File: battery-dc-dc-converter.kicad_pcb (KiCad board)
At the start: 2 copper layers, 42 x 31 mm, 18 parts, among them J1 Conn_01x02, J2 Conn_01x02, U1 LMR16030

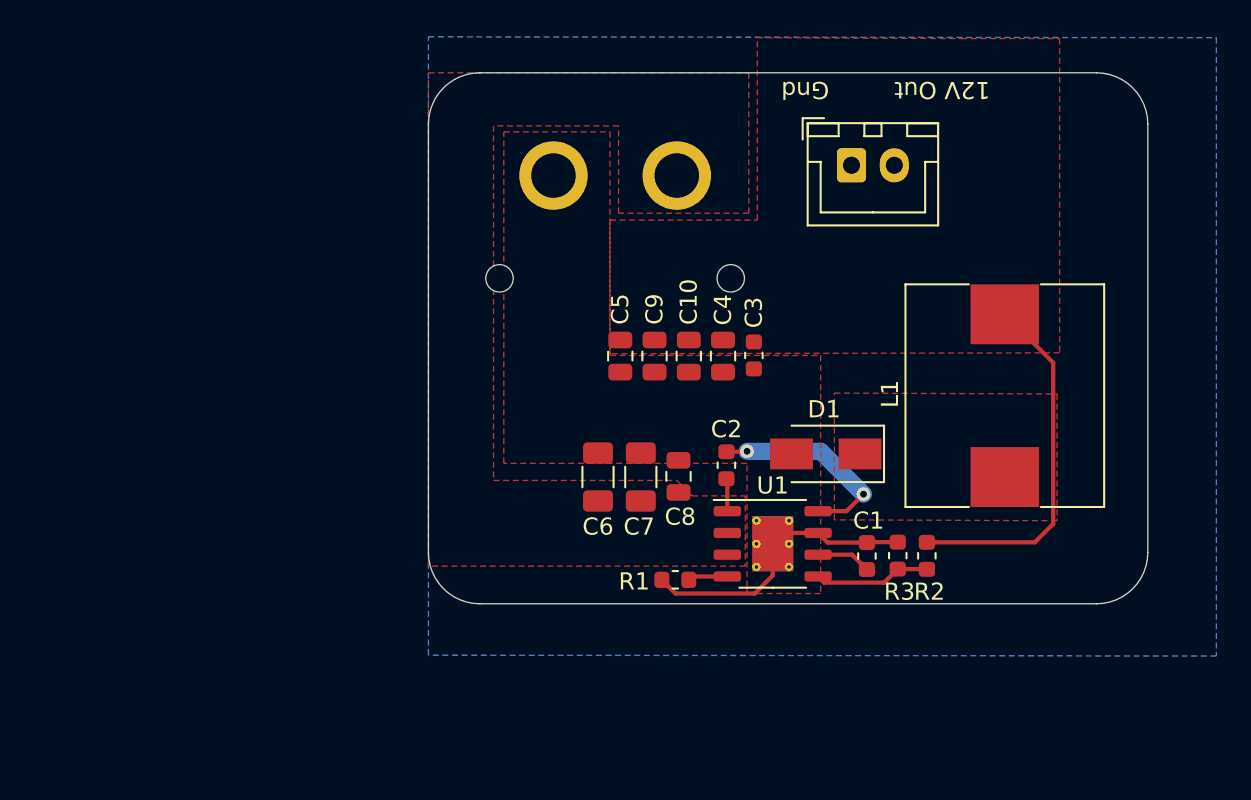
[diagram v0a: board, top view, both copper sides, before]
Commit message: Added fuses
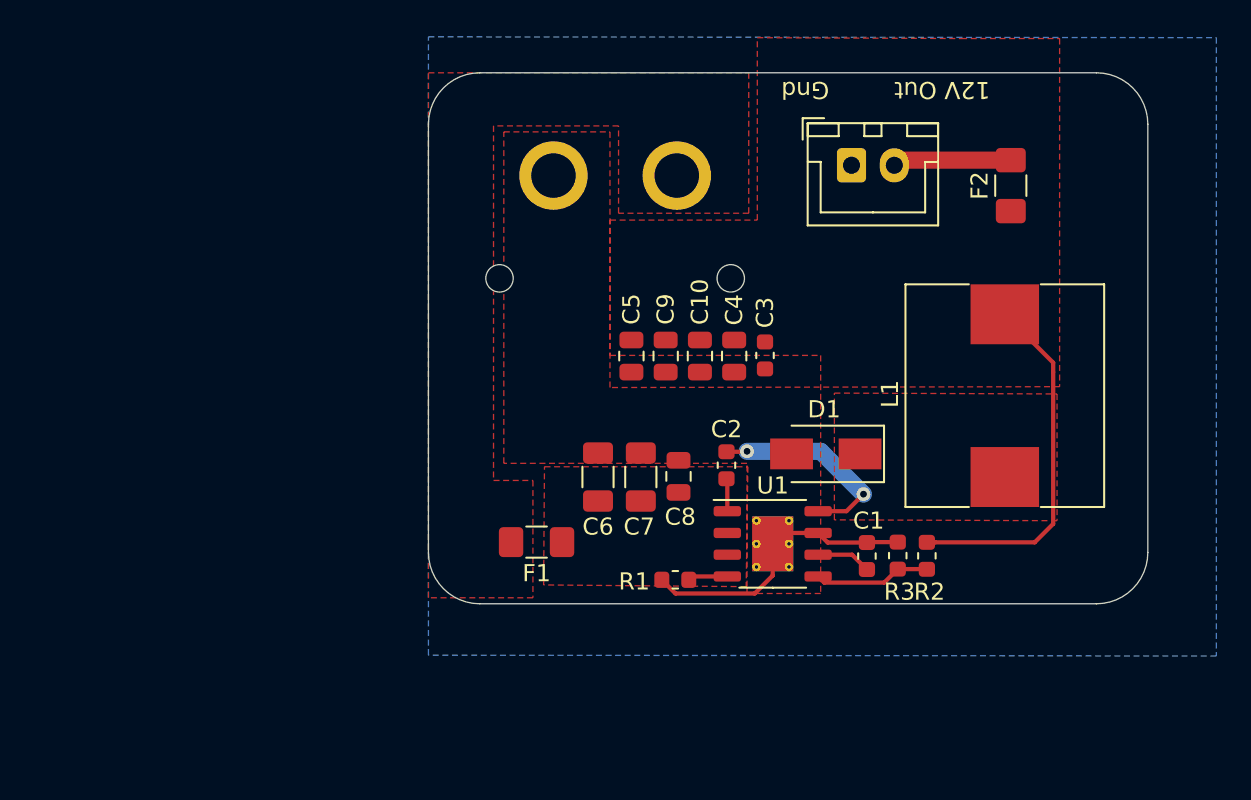
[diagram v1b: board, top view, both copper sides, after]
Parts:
- added F1: 1A, Fuse:Fuse_1206_3216Metric_Pad1.42x1.75mm_HandSolder, F.Cu at (106.3, 63.4)
- added F2: 3A, Fuse:Fuse_1206_3216Metric_Pad1.42x1.75mm_HandSolder, F.Cu at (134.0, 42.6)
- moved C3 0.65 mm to (119.7, 52.5)
- moved C10 0.65 mm to (115.8, 52.5)
- moved C4 0.65 mm to (117.8, 52.5)
- moved C5 0.65 mm to (111.8, 52.5)
- moved C9 0.65 mm to (113.8, 52.5)
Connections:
- J1 pad 2: VCC -> Net-(F1-Pad2)
- J2 pad 2: +12V -> Net-(F2-Pad2)
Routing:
- net Net-(F2-Pad2): track 0.00 -> 6.92 mm
- added copper zone on F.Cu, net Net-(F1-Pad2)

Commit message: Added low voltage protection
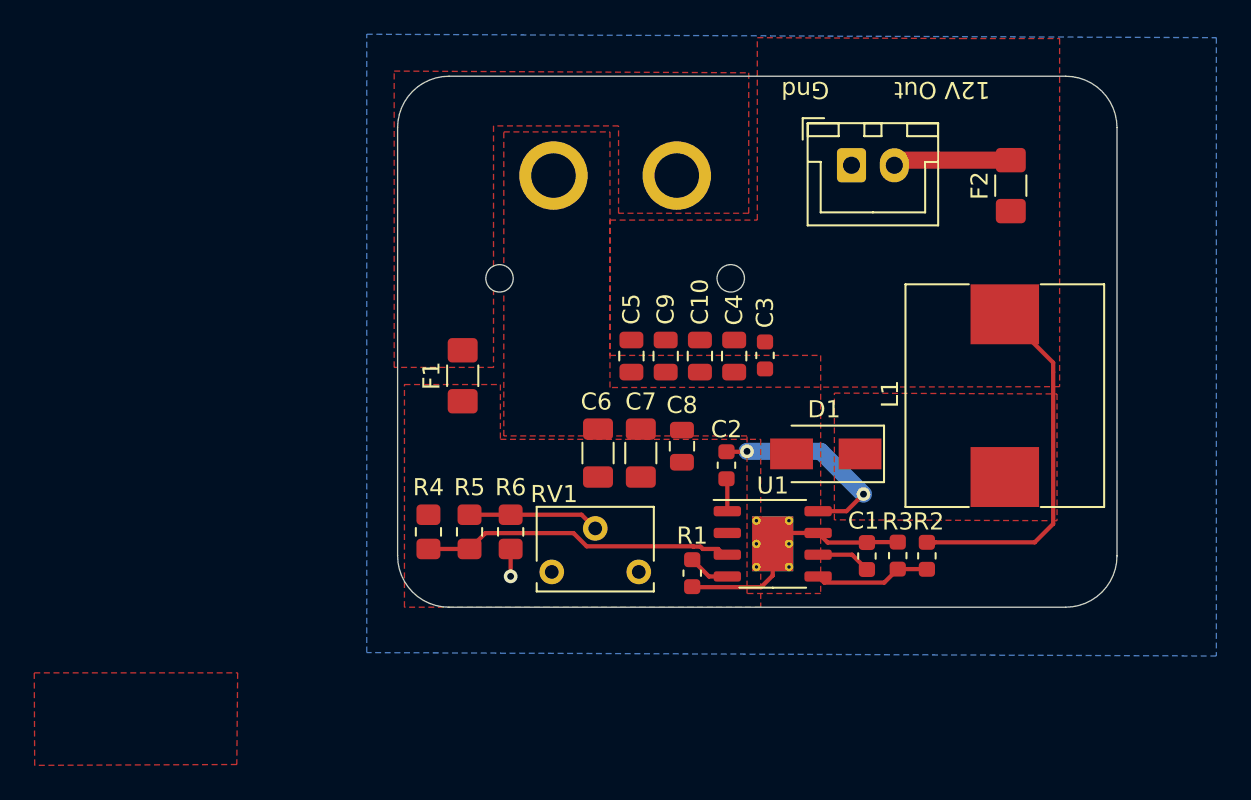
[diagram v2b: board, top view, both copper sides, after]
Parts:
- added R4: 560K, Resistor_SMD:R_0805_2012Metric_Pad1.20x1.40mm_HandSolder, F.Cu at (100.0, 62.8)
- added R5: 18K, Resistor_SMD:R_0805_2012Metric_Pad1.20x1.40mm_HandSolder, F.Cu at (102.4, 62.8)
- added R6: R, Resistor_SMD:R_0805_2012Metric_Pad1.20x1.40mm_HandSolder, F.Cu at (104.8, 62.8)
- added RV1: 10K, Potentiometer_THT:Potentiometer_Vishay_T73XX_Horizontal, F.Cu at (107.2, 65.1)
- moved F1 10.6 mm to (102.0, 53.7), turned to 90 degrees
- moved C8 1.77 mm to (114.8, 57.8)
- moved C6 1.40 mm to (109.9, 58.2)
- moved C7 1.40 mm to (112.4, 58.2)
- moved R1 1.06 mm to (115.4, 65.2), turned to 270 degrees
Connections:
- U1 pad 3: VCC -> Net-(R4-Pad2)
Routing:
- net Net-(R4-Pad2): track 0.00 -> 18.5 mm
- net Net-(R5-Pad2): track 0.00 -> 7.67 mm
- net GND: track 16.9 -> 16.5 mm, vias 0 -> 1

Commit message: Added panelized layout
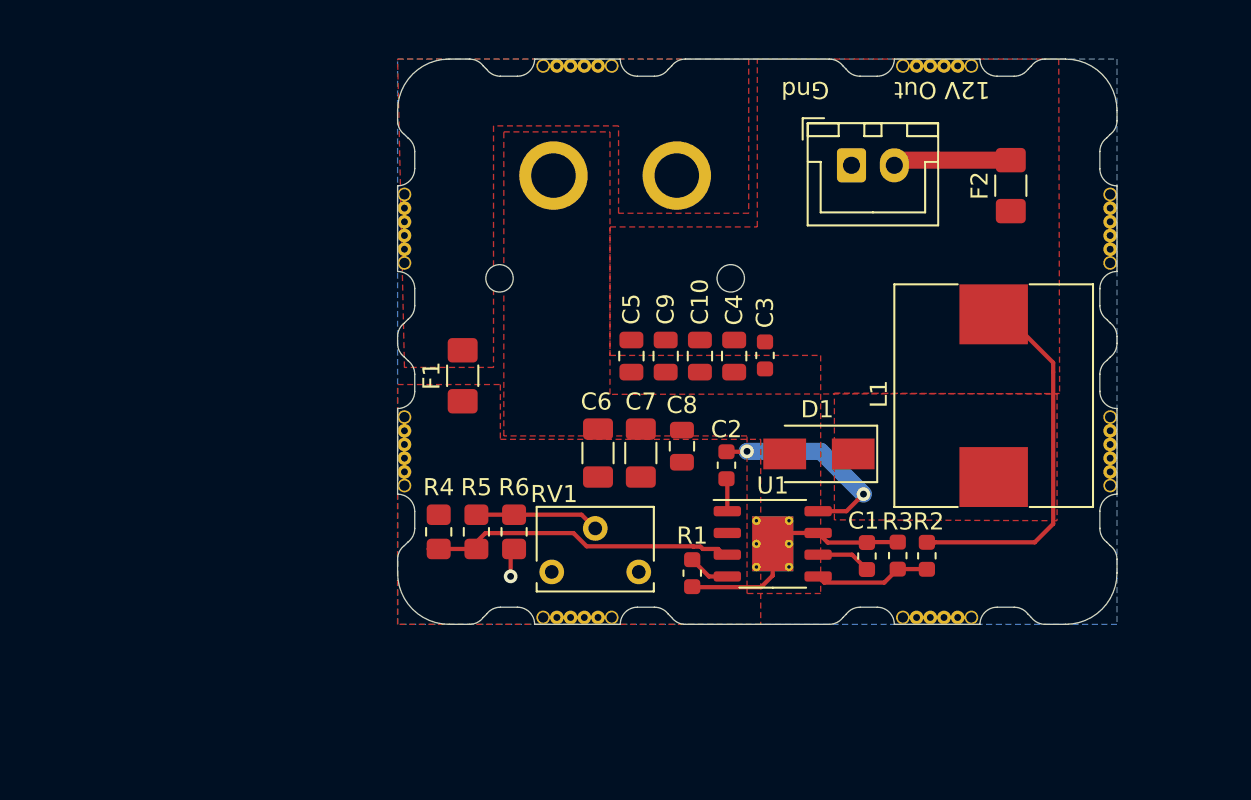
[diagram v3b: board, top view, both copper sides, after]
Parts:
- added REF**: mousebite, scooter-ps:mousebite, F.Cu at (103.2, 35.2)
- added REF**: mousebite, scooter-ps:mousebite, F.Cu at (124.2, 35.2)
- added REF**: mousebite, scooter-ps:mousebite, F.Cu at (140.2, 39.6)
- added REF**: mousebite, scooter-ps:mousebite, F.Cu at (140.2, 52.6)
- added REF**: mousebite, scooter-ps:mousebite, F.Cu at (135.2, 68.2)
- added REF**: mousebite, scooter-ps:mousebite, F.Cu at (114.2, 68.2)
- added REF**: mousebite, scooter-ps:mousebite, F.Cu at (98.2, 63.6)
- added REF**: mousebite, scooter-ps:mousebite, F.Cu at (98.2, 50.6)
- moved L1 0.65 mm to (133.0, 54.9)
- moved R4 0.60 mm to (100.6, 62.8)
- moved D1 0.40 mm to (122.8, 58.2)
- moved R5 0.40 mm to (102.8, 62.8)
- moved R6 0.20 mm to (105.0, 62.8)
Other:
- board size 42 x 31 mm -> 42 x 33 mm

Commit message: Updateed power pads, on/off resistors.
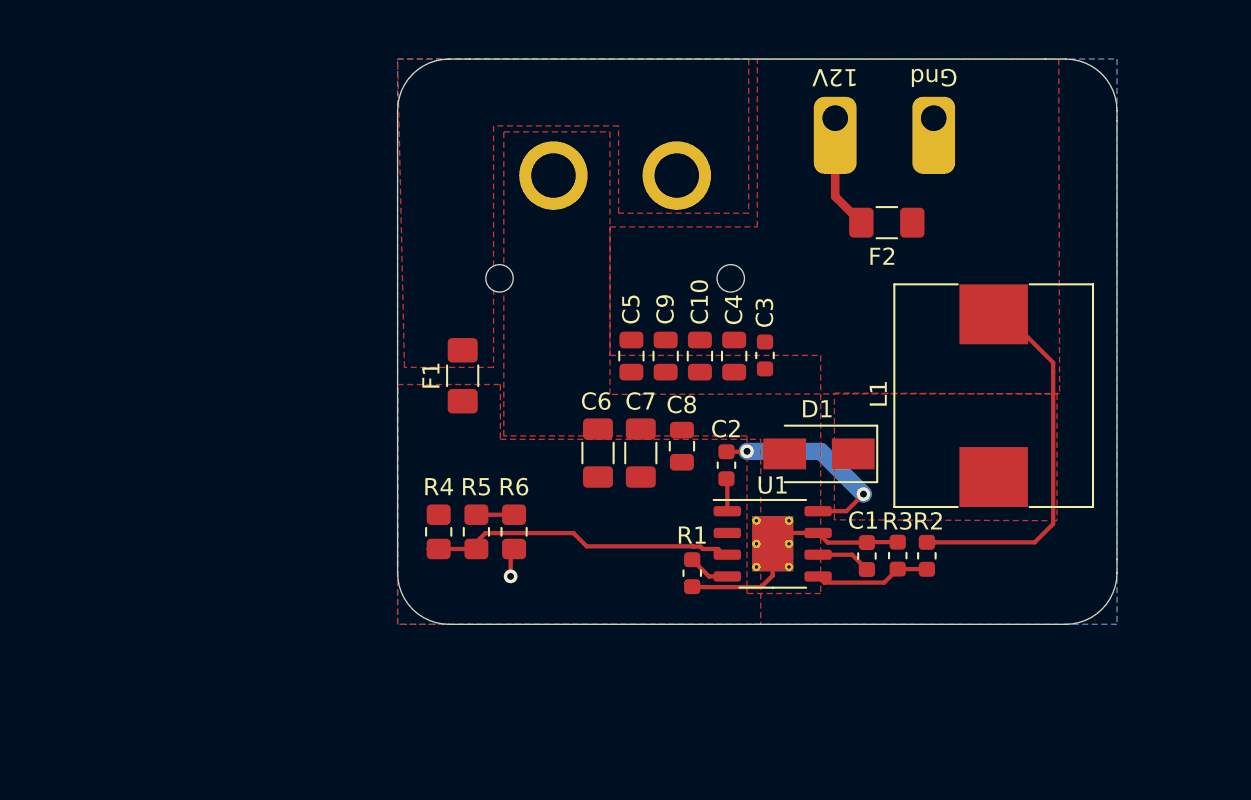
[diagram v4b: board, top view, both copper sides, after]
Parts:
- removed REF** (x8): mousebite, scooter-ps:mousebite
- removed RV1: 10K, Potentiometer_THT:Potentiometer_Vishay_T73XX_Horizontal
- added J3: Conn_01x01, battery-dc-dc-converter:hole-pad, F.Cu at (129.5, 38.8)
- F1: value 1A -> 3A
- J2: value Conn_01x02 -> Conn_01x01; footprint Connector_JST:JST_XH_B2B-XH-A_1x02_P2.50mm_Vertical -> battery-dc-dc-converter:hole-pad
- R4: value 560K -> 1M
- R5: value 18K -> 33K
- R6: value R -> 3k9
- moved F2 7.55 mm to (126.8, 44.8), turned to 0 degrees
- moved J2 2.82 mm to (123.8, 38.8)
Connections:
- F2 pad 1: +12V -> Net-(F2-Pad1)
- F2 pad 2: Net-(F2-Pad2) -> +12V
- J2 pad 1: GND -> Net-(F2-Pad1)
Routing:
- net Net-(F2-Pad1): track 0.00 -> 7.09 mm
- net Net-(F2-Pad2): track 6.92 -> 0.00 mm
- net Net-(R5-Pad2): track 7.67 -> 2.40 mm
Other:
- outline, holes or cut-outs redrawn
- board text added: "12V"
- board text removed: "12V Out"

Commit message: Panalized PCBs
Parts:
- moved J2 0.75 mm to (123.8, 39.5)
- moved J3 0.75 mm to (129.5, 39.5)
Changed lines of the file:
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@@
     (pad_to_mask_clearance 0.05)
     (aux_axis_origin 0 0)
+    (grid_origin 98.25 35.25)
     (visible_elements FFFFFF7F)
     (pcbplotparams
       (layerselection 0x010fc_ffffffff)
-      (usegerberextensions false)
+      (usegerberextensions true)
       (usegerberattributes true)
       (usegerberadvancedattributes true)
@@
       (viasonmask false)
       (mode 1)
-      (useauxorigin false)
+      (useauxorigin true)
       (hpglpennumber 1)
       (hpglpenspeed 20)
@@
       (drillshape 0)
       (scaleselection 1)
-      (outputdirectory "fabrication-output/v2/"))
+      (outputdirectory "fabrication-output/v3/"))
   )
   (net 0 "")
@@
   )
   (module battery-dc-dc-converter:hole-pad (layer F.Cu)
-    (at 129.5 38.75)
+    (at 129.5 39.5)
     (fp_text reference J3 (at 0 0.5) (layer F.SilkS) hide
       (effects (font (size 1 1) (thickness 0.15)))
@@
       (effects (font (size 1 1) (thickness 0.15)))
     )
-    (pad 1 thru_hole roundrect (at 0 -0.1) (size 2.5 4.5) (drill 1.5 (offset 0 1)) (layers *.Cu *.Mask) (roundrect_rratio 0.25)
+    (pad 1 thru_hole roundrect (at 0 -0.1) (size 2.5 4.5) (drill 1.5) (layers *.Cu *.Mask) (roundrect_rratio 0.25)
       (net 2 GND))
   )
   (module battery-dc-dc-converter:hole-pad (layer F.Cu)
-    (at 123.75 38.75)
+    (at 123.75 39.5)
     (fp_text reference J2 (at 0 0.5) (layer F.SilkS) hide
       (effects (font (size 1 1) (thickness 0.15)))
@@
       (effects (font (size 1 1) (thickness 0.15)))
     )
-    (pad 1 thru_hole roundrect (at 0 -0.1) (size 2.5 4.5) (drill 1.5 (offset 0 1)) (layers *.Cu *.Mask) (roundrect_rratio 0.25)
+    (pad 1 thru_hole roundrect (at 0 -0.1) (size 2.5 4.5) (drill 1.5) (layers *.Cu *.Mask) (roundrect_rratio 0.25)
       (net 12 "Net-(F2-Pad1)"))
   )

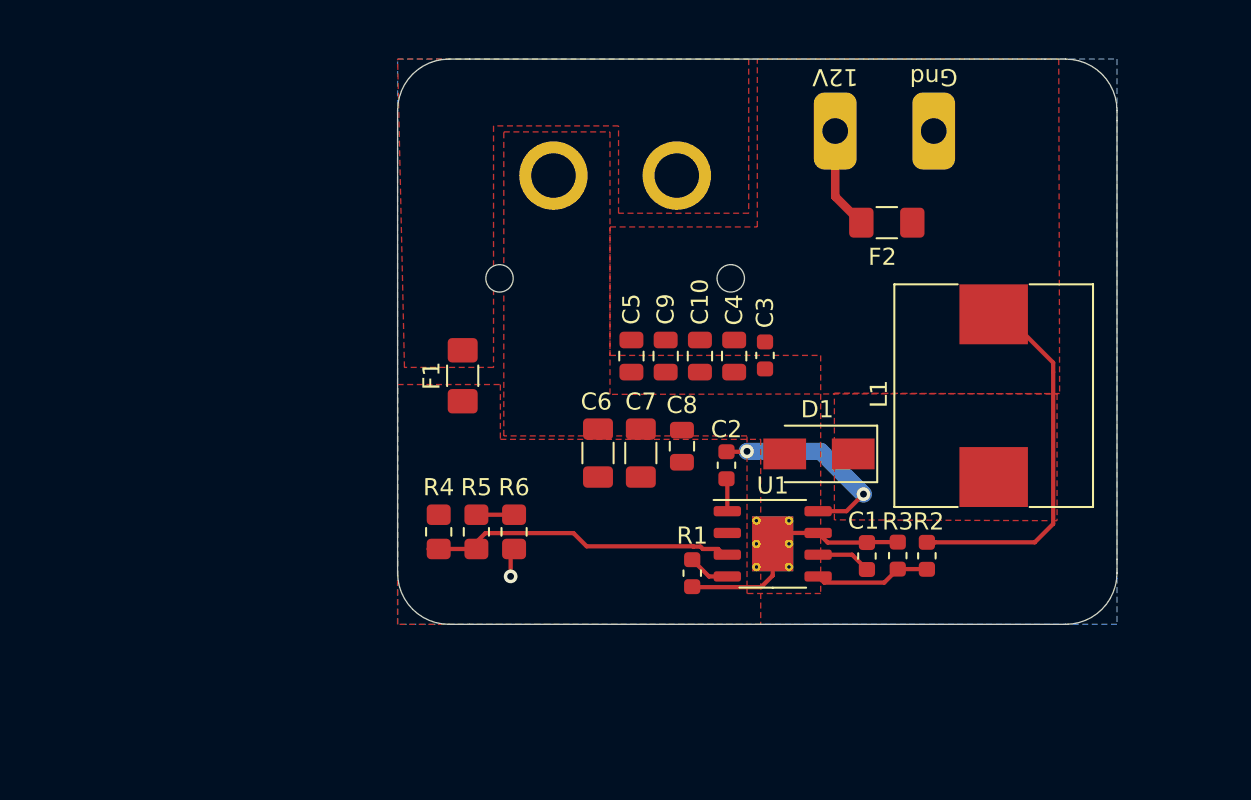
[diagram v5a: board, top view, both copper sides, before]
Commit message: Added recessed nibbles
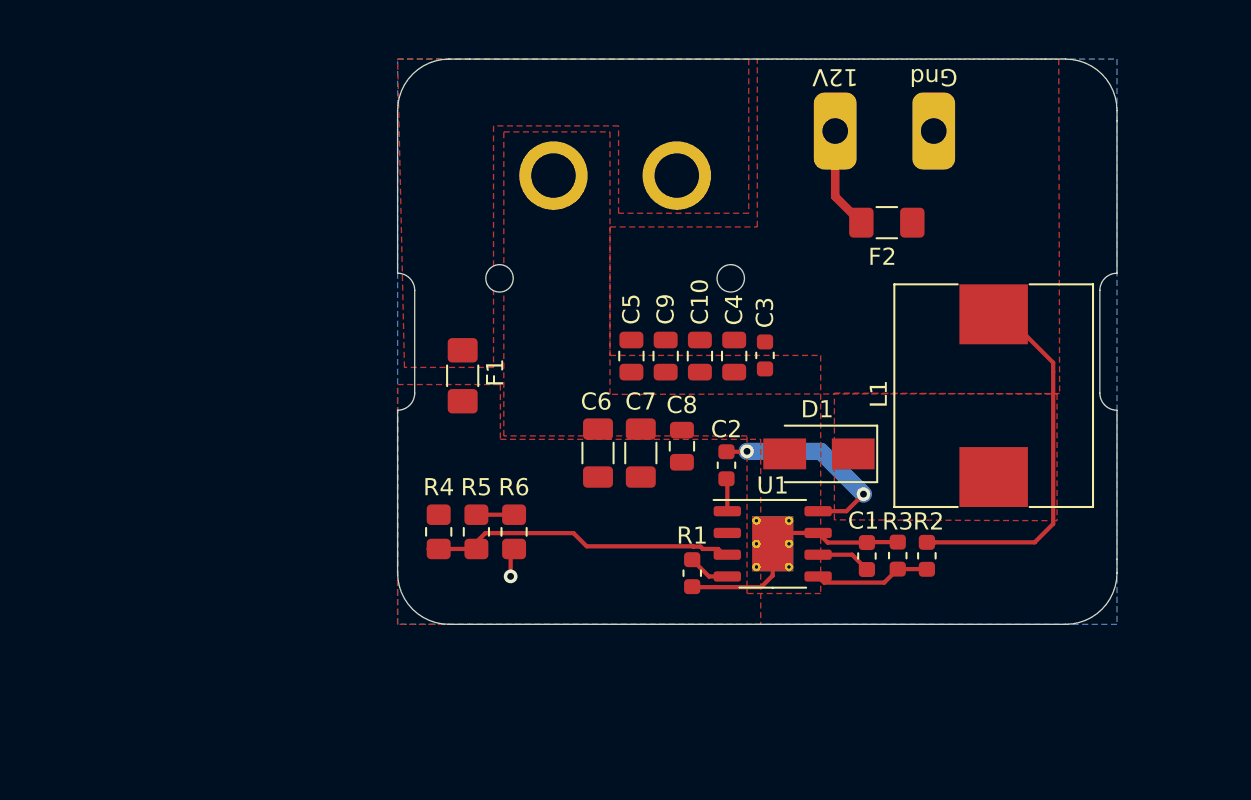
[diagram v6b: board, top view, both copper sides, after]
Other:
- outline, holes or cut-outs redrawn
